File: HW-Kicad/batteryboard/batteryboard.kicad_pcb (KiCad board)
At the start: 2 copper layers, 101 x 101 mm, 9 parts, among them J1 Conn_01x05_Male, J2 Conn_01x01_Male, J3 Conn_01x01_Male, J4 Conn_01x01_Male, J5 Conn_01x01_Male, J6 Conn_01x01_Male, J7 Conn_01x02_Male, U1 YAAJ_DCDC_StepDown_LM2596

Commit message: version final de la batery board
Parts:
- added REF**: plastico, soporteplasticobaterias:plastico, F.Cu at (117.4, 133.9)
- J7: footprint Connector_Molex:Molex_KK-254_AE-6410-02A_1x02_P2.54mm_Vertical -> Connector_Molex:Molex_KK-254_AE-6410-03A_1x03_P2.54mm_Vertical
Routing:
- net Net-(F1-Pad2): track 46.3 -> 115.5 mm
- net Net-(U1-Pad4): track 24.8 -> 27.0 mm

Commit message: version final de placa baterías
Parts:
- removed REF**: plastico, soporteplasticobaterias:plastico
- removed U1: YAAJ_DCDC_StepDown_LM2596, LM2596:YAAJ_DCDC_StepDown_LM2596
- added F2: Fuse, Fuse:Fuseholder_Blade_Mini_Keystone_3568, F.Cu at (113.7, 73.3)
- added J8: Conn_01x02_Male, TerminalBlock:TerminalBlock_bornier-2_P5.08mm, F.Cu at (112.5, 96.0)
- added J9: Conn_01x02_Male, TerminalBlock:TerminalBlock_bornier-2_P5.08mm, F.Cu at (112.5, 111.3)
- added Q1: ATP213, Package_TO_SOT_SMD:TO-252-2, B.Cu at (125.0, 96.0)
- added Q2: ATP213, Package_TO_SOT_SMD:TO-252-2, B.Cu at (125.0, 111.3)
- added R1: 10k, Resistor_THT:R_Axial_DIN0207_L6.3mm_D2.5mm_P10.16mm_Horizontal, B.Cu at (133.6, 83.3)
- added R2: 100k, Resistor_THT:R_Axial_DIN0207_L6.3mm_D2.5mm_P10.16mm_Horizontal, B.Cu at (137.7, 103.6)
- added R3: 10k, Resistor_THT:R_Axial_DIN0207_L6.3mm_D2.5mm_P10.16mm_Horizontal, B.Cu at (133.6, 98.8)
- added R4: 100k, Resistor_THT:R_Axial_DIN0207_L6.3mm_D2.5mm_P10.16mm_Horizontal, B.Cu at (137.7, 119.1)
- moved F1 89.4 mm to (203.1, 91.1)
- moved J7 2.61 mm to (160.5, 139.9)
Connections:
- J7 pad 1: GND -> Net-(F1-Pad2)
- J7 pad 2: Net-(U1-Pad4) -> abortSig
- J7 pad 3: Net-(F1-Pad2) -> GND
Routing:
- net GND: track 90.7 -> 192.9 mm
- net abortSig: track 0.00 -> 88.2 mm
- net Net-(F1-Pad1): track 73.8 -> 141.0 mm
- net Net-(F1-Pad2): track 115.5 -> 75.7 mm
- net Net-(F2-Pad2): track 0.00 -> 30.3 mm
- net Net-(U1-Pad4): track 27.0 -> 0.00 mm
- net Net-(J8-Pad1): track 0.00 -> 10.4 mm
- net Net-(J9-Pad1): track 0.00 -> 10.3 mm
- net Net-(Q1-Pad1): track 0.00 -> 8.54 mm
- net Net-(Q2-Pad1): track 0.00 -> 8.50 mm
- net Net-(J1-Pad2): track 14.8 -> 15.4 mm
- added copper zone on B.Cu, net Net-(F1-Pad1)
- removed copper zone on F.Cu, net GND
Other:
- board text removed: "+-"
- board text removed: "12V_OUT"

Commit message: cambie para tener dos señales de  control distintas
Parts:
- J7: value Conn_01x02_Male -> Conn_01x04_Male; footprint Connector_Molex:Molex_KK-254_AE-6410-03A_1x03_P2.54mm_Vertical -> Connector_Molex:Molex_KK-254_AE-6410-04A_1x04_P2.54mm_Vertical
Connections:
- J7 pad 3: GND -> parachuteSIG
- R3 pad 1: abortSig -> parachuteSIG
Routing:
- net parachuteSIG: track 0.00 -> 60.3 mm
- net abortSig: track 88.2 -> 77.5 mm

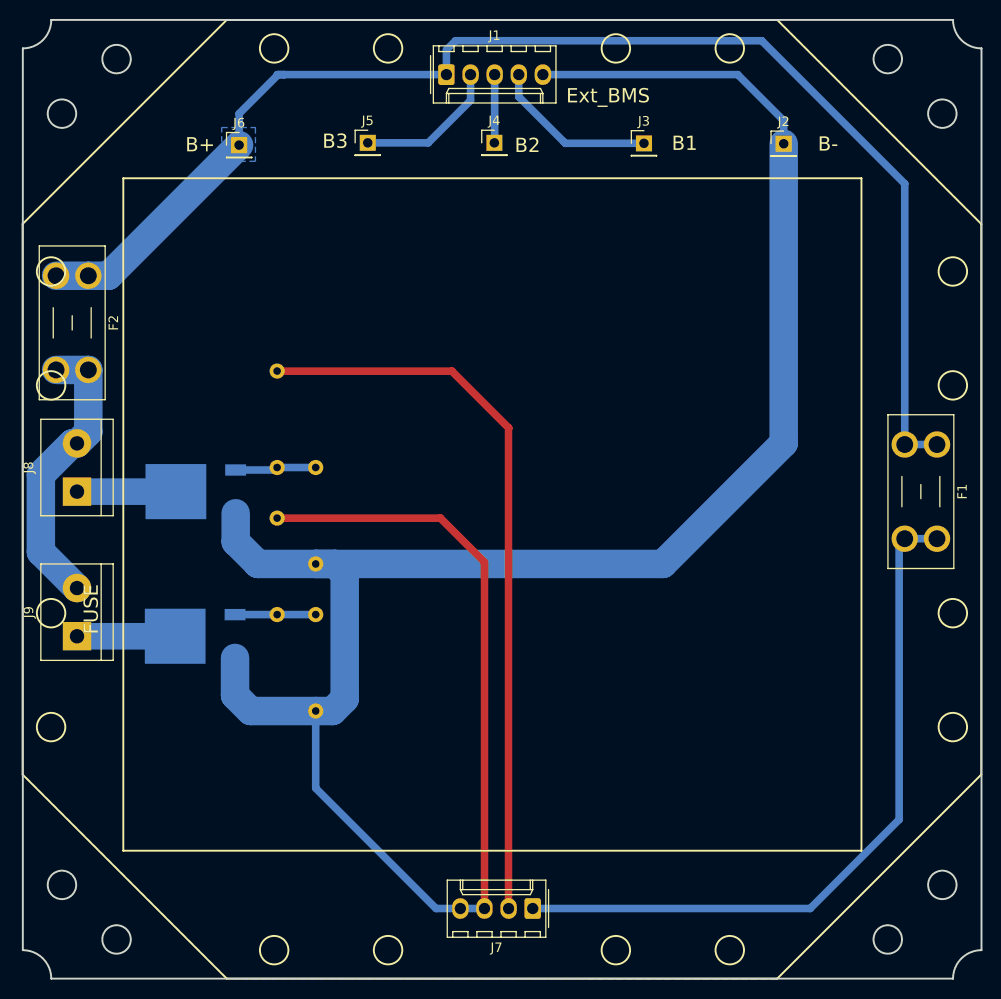
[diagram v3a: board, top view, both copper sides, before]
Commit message: agregue pines de baterías para aprs
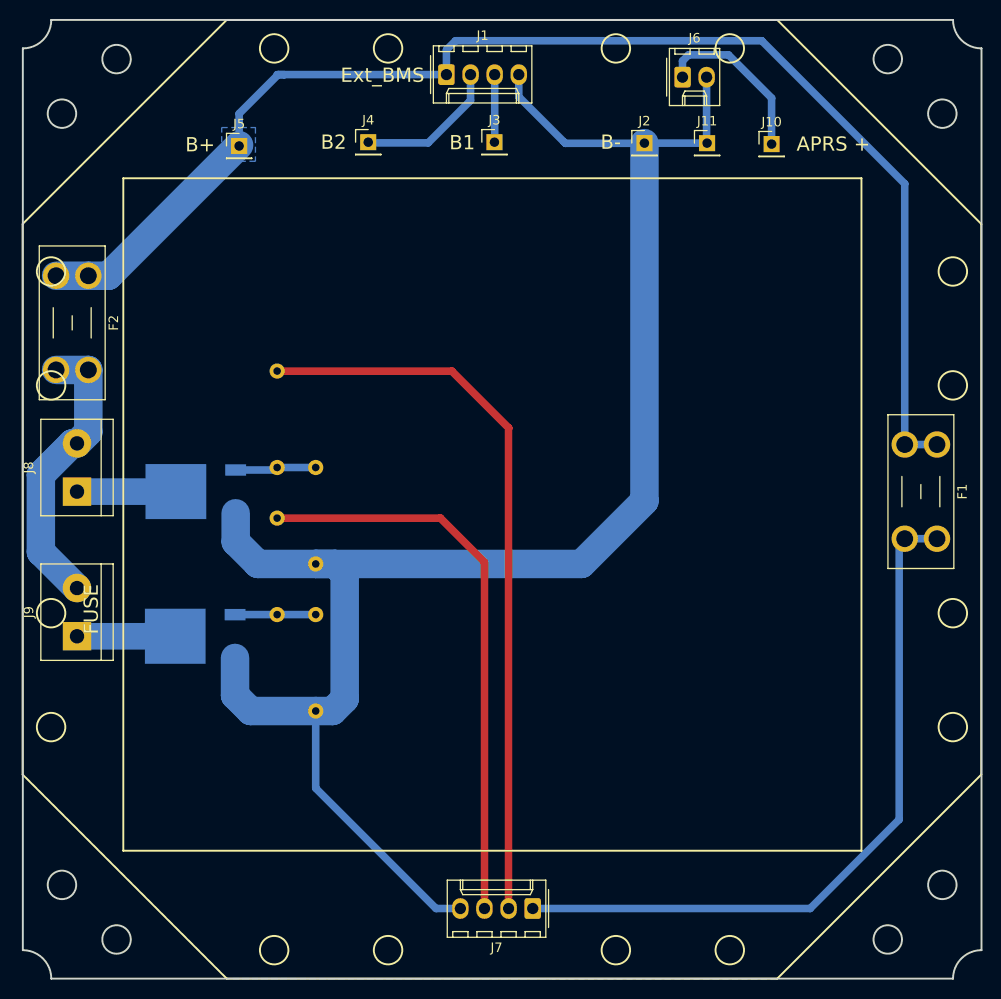
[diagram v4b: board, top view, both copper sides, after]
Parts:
- added J10: Conn_01x01_Male, Connector_PinHeader_2.54mm:PinHeader_1x01_P2.54mm_Vertical, F.Cu at (185.7, 59.4)
- added J11: Conn_01x01_Male, Connector_PinHeader_2.54mm:PinHeader_1x01_P2.54mm_Vertical, F.Cu at (178.9, 59.3)
- J1: value Conn_01x05_Male -> Conn_01x04_Male; footprint Connector_Molex:Molex_KK-254_AE-6410-05A_1x05_P2.54mm_Vertical -> Connector_Molex:Molex_KK-254_AE-6410-04A_1x04_P2.54mm_Vertical
- J6: value Conn_01x01_Male -> Conn_01x02_Male; footprint Connector_PinHeader_2.54mm:PinHeader_1x01_P2.54mm_Vertical -> Connector_Molex:Molex_KK-254_AE-6410-02A_1x02_P2.54mm_Vertical
- moved J6 47.3 mm to (176.3, 52.4)
- moved J3 15.8 mm to (156.5, 59.2)
- moved J2 14.7 mm to (172.3, 59.3)
- moved J5 13.6 mm to (129.6, 59.6)
- moved J4 13.3 mm to (143.2, 59.2)
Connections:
- J1 pad 4: Net-(J1-Pad4) -> GND
- J3 pad 1: Net-(J1-Pad4) -> Net-(J1-Pad3)
- J4 pad 1: Net-(J1-Pad3) -> Net-(J1-Pad2)
- J5 pad 1: Net-(J1-Pad2) -> Net-(F1-Pad1)
- J6 pad 1: Net-(F1-Pad1) -> Net-(J10-Pad1)
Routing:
- net Net-(J10-Pad1): track 0.00 -> 18.1 mm
- net Net-(J1-Pad4): track 17.6 -> 0.00 mm
- net GND: track 192.9 -> 180.6 mm
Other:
- board text added: "APRS +"
- board text removed: "B3"
